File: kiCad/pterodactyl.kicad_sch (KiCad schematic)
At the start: 145 parts, among them J0 Conn_01x03, SW0 MX, SW1 MX, SW10 MX, SW11 MX, SW12 MX, SW13 MX, SW14 MX, SW15 MX, SW16 MX, SW17 MX, SW18 MX, SW19 MX, SW2 MX, SW20 MX, SW21 MX, SW22 MX, SW23 MX, SW24 MX, SW25 MX, SW26 MX, SW27 MX, SW28 MX, SW29 MX, SW3 MX, SW30 MX, SW31 MX, SW32 MX, SW33 MX, SW34 MX, SW35 MX, SW36 MX, SW37 MX, SW38 MX, SW39 MX, SW4 MX, SW40 MX, SW41 MX, SW42 MX, SW43 MX, SW44 MX, SW45 MX, SW46 MX, SW47 MX, SW48 MX, SW49 MX, SW5 MX, SW50 MX, SW51 MX, SW52 MX, SW53 MX, SW54 MX, SW55 MX, SW56 MX, SW57 MX, SW58 MX, SW59 MX, SW6 MX, SW60 MX, SW61 RotaryEncoder_Switch, SW62 MX, SW63 MX, SW64 MX, SW65 MX, SW66 MX, SW67 MX, SW68 MX, SW69 MX, SW7 MX, SW70 MX, SW71 MX, SW8 MX, SW9 MX, U0 Sparkfun_Pro_Micro

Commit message: finish routing
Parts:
- renumbered D60 to D12, D61 to D13, D62 to D14, D12 to D15, D13 to D16, D14 to D17, D15 to D18, D16 to D19, D17 to D20, D18 to D21, D19 to D22, D20 to D23, D21 to D24, D22 to D25, D23 to D26, D63 to D27, D64 to D28, D65 to D29, D70 to D30, D24 to D31, D25 to D32, D26 to D33, D27 to D34, D28 to D35, D29 to D36, D30 to D37, D31 to D38, D32 to D39, D33 to D40, D34 to D41, D35 to D42, D66 to D43, D67 to D44, D68 to D45, D69 to D46, D36 to D47, D37 to D48, D38 to D49, D39 to D50, D40 to D51, D41 to D52, D42 to D53, D43 to D54, D44 to D55, D45 to D56, D46 to D57, D47 to D58, D48 to D59, D49 to D60, D50 to D61, D51 to D62, D52 to D63, D53 to D64, D54 to D65, D55 to D66, D56 to D67, D57 to D68, D58 to D69, D59 to D70, SW1 to SW0, SW2 to SW1, SW11 to SW10, SW12 to SW11, SW62 to SW12, SW63 to SW13, SW64 to SW14, SW61 to SW15, SW13 to SW16, SW14 to SW17, SW15 to SW18, SW16 to SW19, SW3 to SW2, SW17 to SW20, SW18 to SW21, SW19 to SW22, SW20 to SW23, SW21 to SW24, SW22 to SW25, SW23 to SW26, SW24 to SW27, SW65 to SW28, SW66 to SW29, SW4 to SW3, SW67 to SW30, SW25 to SW31, SW26 to SW32, SW27 to SW33, SW28 to SW34, SW29 to SW35, SW30 to SW36, SW31 to SW37, SW32 to SW38, SW33 to SW39, SW5 to SW4, SW34 to SW40, SW35 to SW41, SW36 to SW42, SW68 to SW43, SW69 to SW44, SW70 to SW45, SW71 to SW46, SW37 to SW47, SW38 to SW48, SW39 to SW49, SW6 to SW5, SW40 to SW50, SW41 to SW51, SW42 to SW52, SW43 to SW53, SW44 to SW54, SW45 to SW55, SW46 to SW56, SW47 to SW57, SW48 to SW58, SW49 to SW59, SW7 to SW6, SW50 to SW60, SW51 to SW61, SW52 to SW62, SW53 to SW63, SW54 to SW64, SW55 to SW65, SW56 to SW66, SW57 to SW67, SW58 to SW68, SW59 to SW69, SW8 to SW7, SW60 to SW70, SW0 to SW71, SW9 to SW8, SW10 to SW9
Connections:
- net COL2: now also U0.18 (D19/A1); no longer U0.12 (~D9/A9)
- net COL3: now also U0.9 (~D6/A7); no longer U0.11 (D8/A8)
- net COL5: now also U0.11 (D8/A8); no longer U0.9 (~D6/A7)
- net COL6: now also SW13.1, SW29.1, SW44.1
- net COL7: now also SW14.1, SW15.S2, SW30.1, SW45.1, SW46.1; no longer SW13.1, SW29.1, SW44.1
- net ROTA: now also U0.5 (D2); no longer U0.1 (D1/TX)
- net ROW0: now also U0.12 (~D9/A9); no longer U0.18 (D19/A1)
- net ROW3: now also U0.15 (D14); no longer U0.14 (D16)
- net ROW4: now also U0.14 (D16); no longer U0.13 (~D10/A10)
- net COL8 renamed ROW2
- net ROW2: now also U0.13 (~D10/A10); no longer SW14.1, SW15.S2, SW30.1, SW45.1, SW46.1, U0.15 (D14), U0.6 (~D3)
- no-connect marks 2 -> 1
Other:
- moved on the sheet: SW71, U0

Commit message: add edge cuts, flip controller
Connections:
- net COL0: now also U0.5 (D2); no longer U0.20 (D21/A3)
- net COL1: now also U0.6 (~D3); no longer U0.19 (D20/A2)
- net COL2: now also U0.7 (D4/A6); no longer U0.18 (D19/A1)
- net COL3: now also U0.16 (D15); no longer U0.9 (~D6/A7)
- net COL4: now also U0.15 (D14); no longer U0.10 (D7)
- net COL5: now also U0.14 (D16); no longer U0.11 (D8/A8)
- net COL6: now also U0.17 (D18/A0); no longer U0.8 (~D5)
- net COL7: now also U0.18 (D19/A1); no longer U0.7 (D4/A6)
- net PIN15: now also U0.8 (~D5); no longer U0.17 (D18/A0)
- net ROTA: now also U0.19 (D20/A2); no longer U0.5 (D2)
- net ROTB: now also U0.20 (D21/A3); no longer U0.2 (D0/RX)
- net ROW0: now also U0.13 (~D10/A10); no longer U0.12 (~D9/A9)
- net ROW1: now also U0.9 (~D6/A7); no longer U0.16 (D15)
- net ROW2: now also U0.12 (~D9/A9); no longer U0.13 (~D10/A10)
- net ROW3: now also U0.10 (D7); no longer U0.15 (D14)
- net ROW4: now also U0.11 (D8/A8); no longer U0.14 (D16)
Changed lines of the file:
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@@
 	)
 	(label "COL7"
-		(at 63.5 53.34 180)
-		(fields_autoplaced yes)
-		(effects
-			(font
-				(size 1.27 1.27)
-			)
-			(justify right bottom)
+		(at 93.98 53.34 0)
+		(fields_autoplaced yes)
+		(effects
+			(font
+				(size 1.27 1.27)
+			)
+			(justify left bottom)
 		)
 	)
@@
 	)
 	(label "ROW3"
-		(at 93.98 60.96 0)
-		(fields_autoplaced yes)
-		(effects
-			(font
-				(size 1.27 1.27)
-			)
-			(justify left bottom)
+		(at 63.5 60.96 180)
+		(fields_autoplaced yes)
+		(effects
+			(font
+				(size 1.27 1.27)
+			)
+			(justify right bottom)
 		)
 	)
 	(label "COL0"
-		(at 93.98 48.26 0)
-		(fields_autoplaced yes)
-		(effects
-			(font
-				(size 1.27 1.27)
-			)
-			(justify left bottom)
+		(at 63.5 48.26 180)
+		(fields_autoplaced yes)
+		(effects
+			(font
+				(size 1.27 1.27)
+			)
+			(justify right bottom)
 		)
 	)
 	(label "ROW0"
-		(at 63.5 66.04 180)
-		(fields_autoplaced yes)
-		(effects
-			(font
-				(size 1.27 1.27)
-			)
-			(justify right bottom)
+		(at 93.98 66.04 0)
+		(fields_autoplaced yes)
+		(effects
+			(font
+				(size 1.27 1.27)
+			)
+			(justify left bottom)
 		)
 	)
@@
 	)
 	(label "ROW2"
-		(at 93.98 66.04 0)
-		(fields_autoplaced yes)
-		(effects
-			(font
-				(size 1.27 1.27)
-			)
-			(justify left bottom)
+		(at 63.5 66.04 180)
+		(fields_autoplaced yes)
+		(effects
+			(font
+				(size 1.27 1.27)
+			)
+			(justify right bottom)
 		)
 	)
 	(label "COL5"
-		(at 63.5 63.5 180)
-		(fields_autoplaced yes)
-		(effects
-			(font
-				(size 1.27 1.27)
-			)
-			(justify right bottom)
+		(at 93.98 63.5 0)
+		(fields_autoplaced yes)
+		(effects
+			(font
+				(size 1.27 1.27)
+			)
+			(justify left bottom)
 		)
 	)
@@
 	)
 	(label "COL6"
-		(at 63.5 55.88 180)
-		(fields_autoplaced yes)
-		(effects
-			(font
-				(size 1.27 1.27)
-			)
-			(justify right bottom)
+		(at 93.98 55.88 0)
+		(fields_autoplaced yes)
+		(effects
+			(font
+				(size 1.27 1.27)
+			)
+			(justify left bottom)
 		)
 	)
 	(label "COL3"
+		(at 93.98 58.42 0)
+		(fields_autoplaced yes)
+		(effects
+			(font
+				(size 1.27 1.27)
+			)
+			(justify left bottom)
+		)
+	)
+	(label "ROW1"
 		(at 63.5 58.42 180)
 		(fields_autoplaced yes)
@@
 			)
 			(justify right bottom)
-		)
-	)
-	(label "ROW1"
-		(at 93.98 58.42 0)
-		(fields_autoplaced yes)
-		(effects
-			(font
-				(size 1.27 1.27)
-			)
-			(justify left bottom)
 		)
 	)
@@
 	)
 	(label "ROW4"
-		(at 93.98 63.5 0)
-		(fields_autoplaced yes)
-		(effects
-			(font
-				(size 1.27 1.27)
-			)
-			(justify left bottom)
+		(at 63.5 63.5 180)
+		(fields_autoplaced yes)
+		(effects
+			(font
+				(size 1.27 1.27)
+			)
+			(justify right bottom)
 		)
 	)
 	(label "COL2"
-		(at 93.98 53.34 0)
-		(fields_autoplaced yes)
-		(effects
-			(font
-				(size 1.27 1.27)
-			)
-			(justify left bottom)
+		(at 63.5 53.34 180)
+		(fields_autoplaced yes)
+		(effects
+			(font
+				(size 1.27 1.27)
+			)
+			(justify right bottom)
 		)
 	)
@@
 	)
 	(label "ROTA"
-		(at 63.5 48.26 180)
-		(fields_autoplaced yes)
-		(effects
-			(font
-				(size 1.27 1.27)
-			)
-			(justify right bottom)
+		(at 93.98 50.8 0)
+		(fields_autoplaced yes)
+		(effects
+			(font
+				(size 1.27 1.27)
+			)
+			(justify left bottom)
 		)
 	)
@@
 	)
 	(label "COL4"
-		(at 63.5 60.96 180)
-		(fields_autoplaced yes)
-		(effects
-			(font
-				(size 1.27 1.27)
-			)
-			(justify right bottom)
+		(at 93.98 60.96 0)
+		(fields_autoplaced yes)
+		(effects
+			(font
+				(size 1.27 1.27)
+			)
+			(justify left bottom)
 		)
 	)
@@
 	)
 	(label "COL1"
-		(at 93.98 50.8 0)
-		(fields_autoplaced yes)
-		(effects
-			(font
-				(size 1.27 1.27)
-			)
-			(justify left bottom)
+		(at 63.5 50.8 180)
+		(fields_autoplaced yes)
+		(effects
+			(font
+				(size 1.27 1.27)
+			)
+			(justify right bottom)
 		)
 	)
 	(label "PIN15"
-		(at 93.98 55.88 0)
-		(fields_autoplaced yes)
-		(effects
-			(font
-				(size 1.27 1.27)
-			)
-			(justify left bottom)
+		(at 63.5 55.88 180)
+		(fields_autoplaced yes)
+		(effects
+			(font
+				(size 1.27 1.27)
+			)
+			(justify right bottom)
 		)
 	)
 	(label "ROTB"
-		(at 63.5 40.64 180)
-		(fields_autoplaced yes)
-		(effects
-			(font
-				(size 1.27 1.27)
-			)
-			(justify right bottom)
-		)
-	)
+		(at 93.98 48.26 0)
+		(fields_autoplaced yes)
+		(effects
+			(font
+				(size 1.27 1.27)
+			)
+			(justify left bottom)
+		)
+	)

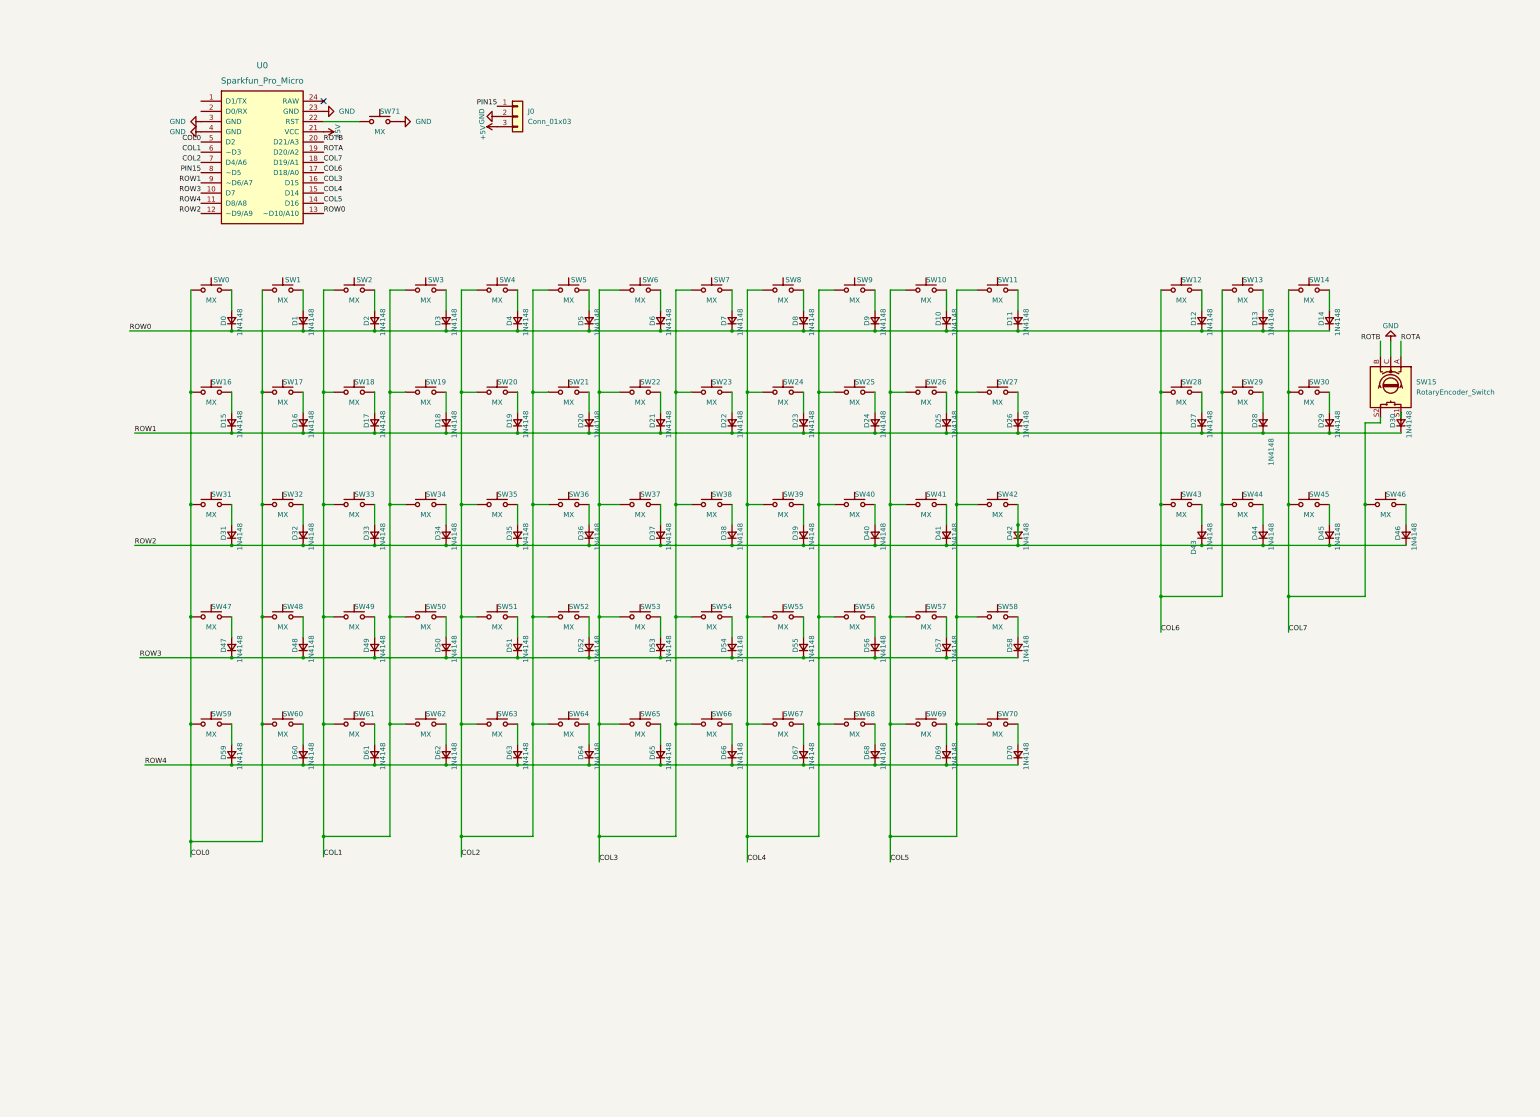
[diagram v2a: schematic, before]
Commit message: rewire everything, change ergonomics
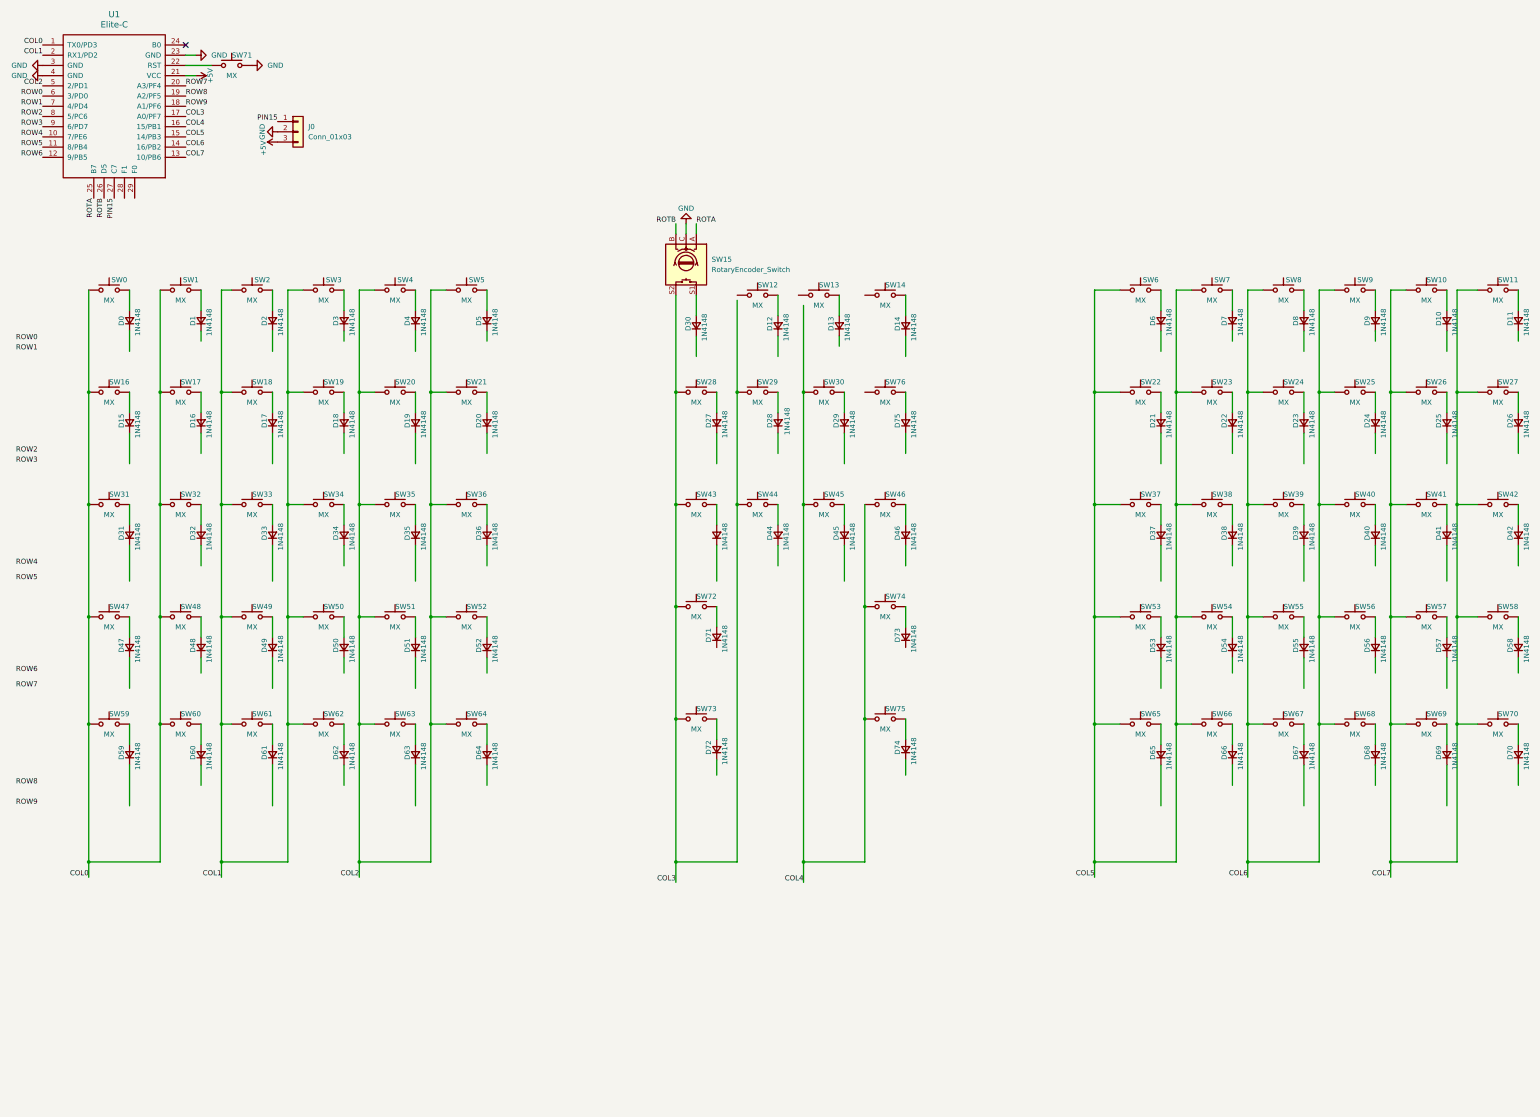
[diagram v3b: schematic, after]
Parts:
- removed U0: Sparkfun_Pro_Micro, Keebio-Parts:ArduinoProMicro, symbol Arduino:Sparkfun_Pro_Micro
- added D71, D72, D73, D74, D75: 1N4148, Diode_THT:D_DO-35_SOD27_P7.62mm_Horizontal, symbol Device:D_Small
- added SW72, SW73, SW74, SW75, SW76: MX, keyswitches:Kailh_socket_MX, symbol Switch:SW_Push
- added U1: Elite-C, Keebio-Parts:Elite-C, symbol keebio:Elite-C
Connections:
- net +5V: now also U1.21 (VCC)
- net COL0: now also U1.1 (TX0/PD3)
- net COL1: now also U1.2 (RX1/PD2)
- net COL2: now also U1.5 (2/PD1)
- net COL3: now also SW15.S2, SW28.1, SW29.1, SW43.1, SW44.1, SW72.1, SW73.1, U1.17 (A0/PF7); no longer SW22.1, SW23.1, SW37.1, SW38.1, SW53.1, SW54.1, SW6.1, SW65.1, SW66.1, SW7.1
- net COL4: now also SW30.1, SW45.1, SW46.1, SW74.1, SW75.1, U1.16 (15/PB1); no longer SW24.1, SW25.1, SW39.1, SW40.1, SW55.1, SW56.1, SW67.1, SW68.1, SW8.1, SW9.1
- net COL5: now also SW22.1, SW23.1, SW37.1, SW38.1, SW53.1, SW54.1, SW6.1, SW65.1, SW66.1, SW7.1, U1.15 (14/PB3); no longer SW10.1, SW11.1, SW26.1, SW27.1, SW41.1, SW42.1, SW57.1, SW58.1, SW69.1, SW70.1
- net COL6: now also SW24.1, SW25.1, SW39.1, SW40.1, SW55.1, SW56.1, SW67.1, SW68.1, SW8.1, SW9.1, U1.14 (16/PB2); no longer SW12.1, SW13.1, SW28.1, SW29.1, SW43.1, SW44.1
- net COL7: now also SW10.1, SW11.1, SW26.1, SW27.1, SW41.1, SW42.1, SW57.1, SW58.1, SW69.1, SW70.1, U1.13 (10/PB6); no longer SW14.1, SW15.S2, SW30.1, SW45.1, SW46.1
- net GND: now also U1.23 (GND), U1.3 (GND), U1.4 (GND)
- net PIN15: now also U1.27 (C7)
- net ROTA: now also U1.25 (B7)
- net ROTB: now also U1.26 (D5)
- net ROW0: now also U1.6 (3/PD0); no longer D0.1 (K), D1.1 (K), D10.1 (K), D11.1 (K), D12.1 (K), D13.1 (K), D14.1 (K), D2.1 (K), D3.1 (K), D4.1 (K), D5.1 (K), D6.1 (K), D7.1 (K), D8.1 (K), D9.1 (K)
- net ROW1: now also U1.7 (4/PD4); no longer D15.1 (K), D16.1 (K), D17.1 (K), D18.1 (K), D19.1 (K), D20.1 (K), D21.1 (K), D22.1 (K), D23.1 (K), D24.1 (K), D25.1 (K), D26.1 (K), D27.1 (K), D28.1 (K), D29.1 (K), D30.1 (K)
- net ROW2: now also U1.8 (5/PC6); no longer D31.1 (K), D32.1 (K), D33.1 (K), D34.1 (K), D35.1 (K), D36.1 (K), D37.1 (K), D38.1 (K), D39.1 (K), D40.1 (K), D41.1 (K), D42.1 (K), D42.2 (A), D43.1 (K), D44.1 (K), D45.1 (K), D46.1 (K), SW42.2
- net ROW3: now also U1.9 (6/PD7); no longer D47.1 (K), D48.1 (K), D49.1 (K), D50.1 (K), D51.1 (K), D52.1 (K), D53.1 (K), D54.1 (K), D55.1 (K), D56.1 (K), D57.1 (K), D58.1 (K)
- net ROW4: now also U1.10 (7/PE6); no longer D59.1 (K), D60.1 (K), D61.1 (K), D62.1 (K), D63.1 (K), D64.1 (K), D65.1 (K), D66.1 (K), D67.1 (K), D68.1 (K), D69.1 (K), D70.1 (K)
- net at SW71.1: now also U1.22 (RST)
- new net: D75.2 (A), SW76.2
- new net: D73.2 (A), SW74.2
- new net: D42.2 (A), SW42.2
- new net: D74.2 (A), SW75.2
- new net: D72.2 (A), SW73.2
- new net: D71.2 (A), SW72.2
- new net ROW5: U1.11 (8/PB4)
- new net ROW6: U1.12 (9/PB5)
- new net ROW7: U1.20 (A3/PF4)
- new net ROW8: U1.19 (A2/PF5)
- new net ROW9: U1.18 (A1/PF6)
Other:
- moved on the sheet: D0, D1, D10, D11, D12, D13, D14, D15, D16, D17, D18, D19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

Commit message: fix annotations, start routing
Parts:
- renumbered D6 to D10, D7 to D11, D8 to D12, D9 to D13, D10 to D14, D11 to D15, D15 to D16, D16 to D17, D17 to D18, D18 to D19, D19 to D20, D20 to D21, D27 to D22, D28 to D23, D29 to D24, D75 to D25, D21 to D26, D22 to D27, D23 to D28, D24 to D29, D25 to D30, D26 to D31, D31 to D32, D32 to D33, D33 to D34, D34 to D35, D35 to D36, D36 to D37, D43 to D38, D44 to D39, D45 to D40, D46 to D41, D37 to D42, D38 to D43, D39 to D44, D40 to D45, D41 to D46, D42 to D47, D47 to D48, D48 to D49, D49 to D50, D50 to D51, D51 to D52, D52 to D53, D71 to D54, D73 to D55, D53 to D56, D54 to D57, D55 to D58, D56 to D59, D30 to D6, D57 to D60, D58 to D61, D59 to D62, D60 to D63, D61 to D64, D62 to D65, D63 to D66, D64 to D67, D72 to D68, D74 to D69, D12 to D7, D65 to D70, D66 to D71, D67 to D72, D68 to D73, D69 to D74, D70 to D75, D13 to D8, D14 to D9, SW6 to SW10, SW7 to SW11, SW8 to SW12, SW9 to SW13, SW10 to SW14, SW11 to SW15, SW28 to SW22, SW29 to SW23, SW30 to SW24, SW76 to SW25, SW22 to SW26, SW23 to SW27, SW24 to SW28, SW25 to SW29, SW26 to SW30, SW27 to SW31, SW31 to SW32, SW32 to SW33, SW33 to SW34, SW34 to SW35, SW35 to SW36, SW36 to SW37, SW43 to SW38, SW44 to SW39, SW45 to SW40, SW46 to SW41, SW37 to SW42, SW38 to SW43, SW39 to SW44, SW40 to SW45, SW41 to SW46, SW42 to SW47, SW47 to SW48, SW48 to SW49, SW49 to SW50, SW50 to SW51, SW51 to SW52, SW52 to SW53, SW72 to SW54, SW74 to SW55, SW53 to SW56, SW54 to SW57, SW55 to SW58, SW56 to SW59, SW15 to SW6, SW57 to SW60, SW58 to SW61, SW59 to SW62, SW60 to SW63, SW61 to SW64, SW62 to SW65, SW63 to SW66, SW64 to SW67, SW73 to SW68, SW75 to SW69, SW12 to SW7, SW65 to SW70, SW66 to SW71, SW67 to SW72, SW68 to SW73, SW69 to SW74, SW70 to SW75, SW71 to SW76, SW13 to SW8, SW14 to SW9, U1 to U0
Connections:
- net COL3: now also SW7.1
- net COL4: now also SW25.1, SW8.1, SW9.1
- net ROW0: now also D1.1 (K), D11.1 (K), D13.1 (K), D15.1 (K), D3.1 (K), D5.1 (K), D7.1 (K), D9.1 (K)
- net ROW1: now also D0.1 (K), D10.1 (K), D12.1 (K), D14.1 (K), D2.1 (K), D4.1 (K), D6.1 (K), D8.1 (K)
- net ROW2: now also D17.1 (K), D19.1 (K), D21.1 (K), D23.1 (K), D25.1 (K), D27.1 (K), D29.1 (K), D31.1 (K)
- net ROW3: now also D16.1 (K), D18.1 (K), D20.1 (K), D22.1 (K), D24.1 (K), D26.1 (K), D28.1 (K), D30.1 (K)
- net ROW4: now also D33.1 (K), D35.1 (K), D37.1 (K), D39.1 (K), D41.1 (K), D43.1 (K), D45.1 (K), D47.1 (K)
- net ROW5: now also D32.1 (K), D34.1 (K), D36.1 (K), D38.1 (K), D40.1 (K), D42.1 (K), D44.1 (K), D46.1 (K)
- net ROW6: now also D49.1 (K), D51.1 (K), D53.1 (K), D55.1 (K), D57.1 (K), D59.1 (K), D61.1 (K)
- net ROW7: now also D48.1 (K), D50.1 (K), D52.1 (K), D54.1 (K), D56.1 (K), D58.1 (K), D60.1 (K)
- net ROW8: now also D63.1 (K), D65.1 (K), D67.1 (K), D69.1 (K), D71.1 (K), D73.1 (K), D75.1 (K)
- net ROW9: now also D62.1 (K), D64.1 (K), D66.1 (K), D68.1 (K), D70.1 (K), D72.1 (K), D74.1 (K)
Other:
- moved on the sheet: D54, D55, D6, D68, D69, D7, D8, D9, J0, SW54, SW55, SW6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
